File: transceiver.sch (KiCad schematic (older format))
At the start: 58 parts

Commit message: Updated with the ttl output
Adding a lot of footprints and other bits.
Changed TVS on USB
Added fuse on USB 5V
TTL level translators, 2x. Go from 3v3 to 1v8, then "anything" to 1v8
for the output.
2x LDO for 3v3->1v8, 3v3->2v5
Plus allow external input.
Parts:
- added C23, C24, C31, C32: 100nF, Capacitor_SMD:C_0603_1608Metric_Pad1.08x0.95mm_HandSolder, symbol Device:C_Small
- added J5: Conn_01x06_Male, Connector_PinHeader_2.54mm:PinHeader_1x06_P2.54mm_Vertical, symbol Connector:Conn_01x06_Male
- added J6, J7, J8: Conn_01x05_Male, Connector_PinHeader_2.54mm:PinHeader_1x05_P2.54mm_Vertical, symbol Connector:Conn_01x05_Male
- added JP15, JP16, JP17, JP18: Jumper, Connector_PinHeader_2.00mm:PinHeader_1x02_P2.00mm_Vertical_SMD_Pin1Left, symbol Device:Jumper
- added R15, R16, R17, R18, R19: 4k7, Connector_PinHeader_2.00mm:PinHeader_1x02_P2.00mm_Vertical_SMD_Pin1Left, symbol Device:R_Small
- added U12, U8: TXS0104EDR, Package_SO:SOIC-14_3.9x8.7mm_P1.27mm, symbol local:TXS0104EDR
- added U7: TLV75525PDBV, Package_TO_SOT_SMD:SOT-23-5, symbol Regulator_Linear:TLV75525PDBV
- added U9: TLV75518PDBV, Package_TO_SOT_SMD:SOT-23-5, symbol Regulator_Linear:TLV75518PDBV
- C19, C20, C21, C22, C25, C26, C27, C28, C29, C30, C33, C34, C35, C36, C37, C38, C39: renamed from C?; footprint (none) -> Capacitor_SMD:C_0603_1608Metric_Pad1.08x0.95mm_HandSolder
- J2, J3, J4, J9: renamed from J?; footprint (none) -> Connector_PinHeader_2.54mm:PinHeader_1x04_P2.54mm_Vertical
- JP1, JP10, JP11, JP12, JP13, JP14, JP19, JP2, JP20, JP21, JP22, JP23, JP24, JP25, JP26, JP3, JP4, JP5, JP6, JP7, JP8, JP9: renamed from JP?; footprint (none) -> Connector_PinHeader_2.00mm:PinHeader_1x02_P2.00mm_Vertical_SMD_Pin1Left
- R10, R11, R12, R13, R14, R9: renamed from R?; footprint (none) -> Connector_PinHeader_2.00mm:PinHeader_1x02_P2.00mm_Vertical_SMD_Pin1Left
- U10, U13, U4, U6: renamed from U?; footprint (none) -> Package_TO_SOT_SMD:SOT-23-6_Handsoldering
- U11, U5: renamed from U?; footprint TSSOP-24 -> Package_SO:TSSOP-24_4.4x7.8mm_P0.65mm
- gave numbers to parts that had none: 1
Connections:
- net +3V3: now also C23.1, JP17.1, R16.1, R17.1, U7.1 (IN), U7.3 (EN), U8.14 (VCCB), U9.1 (IN), U9.3 (EN)
- net CTSn_1: now also U8.10 (B4)
- net GND: now also C23.2, C24.2, C31.2, C32.2, J5.5 (Pin_5), J6.5 (Pin_5), J7.5 (Pin_5), J8.5 (Pin_5), R18.2, R19.2, U12.7 (GND), U7.2 (GND), U8.7 (GND), U9.2 (GND); no longer U13.1, U6.1
- net PORT_2_CTS: now also J6.4 (Pin_4)
- net PORT_2_RTS: now also J6.3 (Pin_3)
- net PORT_2_RXD: now also J6.2 (Pin_2)
- net PORT_2_TXD: now also J6.1 (Pin_1)
- net PORT_3_CTS: now also J7.4 (Pin_4)
- net PORT_3_RTS: now also J7.3 (Pin_3)
- net PORT_3_RXD: now also J7.2 (Pin_2)
- net PORT_3_TXD: now also J7.1 (Pin_1)
- net PORT_4_CTS: now also J8.4 (Pin_4)
- net PORT_4_RTS: now also J8.3 (Pin_3)
- net PORT_4_RXD: now also J8.2 (Pin_2)
- net PORT_4_TXD: now also J8.1 (Pin_1)
- net PWREN#: now also R17.2
- net RTSn_1: now also U8.11 (B3)
- net RXD_1: now also U8.12 (B2)
- net SUSPEND#: now also R16.2
- net TXD_1: now also U8.13 (B1)
- net DADBUS7 renamed DDBUS7
- new net: U12.2 (A1), U8.2 (A1)
- new net: U12.3 (A2), U8.3 (A2)
- new net: U12.4 (A3), U8.4 (A3)
- new net: U12.5 (A4), U8.5 (A4)
- new net: R15.2, U12.8 (OE), U8.8 (OE)
- new net: R18.1, U6.1
- new net: R19.1, U13.1
- new net +1V8: C24.1, C32.1, JP15.1, R15.1, U12.1 (VCCA), U8.1 (VCCA), U9.5 (OUT)
- new net +2V5: JP16.1, U7.5 (OUT)
- new net PORT_1_CTS: J5.4 (Pin_4), U12.10 (B4)
- new net PORT_1_RTS: J5.3 (Pin_3), U12.11 (B3)
- new net PORT_1_RXD: J5.2 (Pin_2), U12.12 (B2)
- new net PORT_1_TXD: J5.1 (Pin_1), U12.13 (B1)
- new net VBUS: JP18.1
- new net VREF: C31.1, J5.6 (Pin_6), JP15.2, JP16.2, JP17.2, JP18.2, U12.14 (VCCB)
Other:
- note added: "Convert the 3v3 Logic to 1v8, then we can do 1v8 to ANY upto 5V on the second stage."
- note added: "Gives direct TTL access\n3v3 bypassing level shifters"
- note added: "Maybe some screw terminals?"
- note added: "Need to generate 2v5 and 1v8 from 3v3\n3v3 and 5v are used as is. OR an external voltage can be used.\nIf no pins are jumpered, then external is the ref.\n\n"

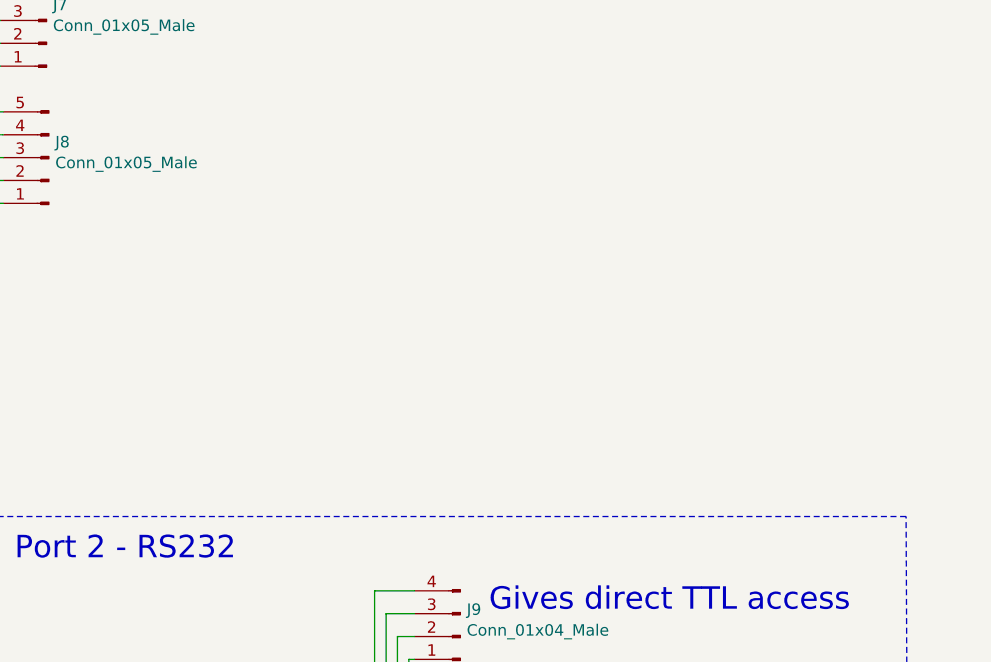
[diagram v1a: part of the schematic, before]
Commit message: Adding some LED stuff.
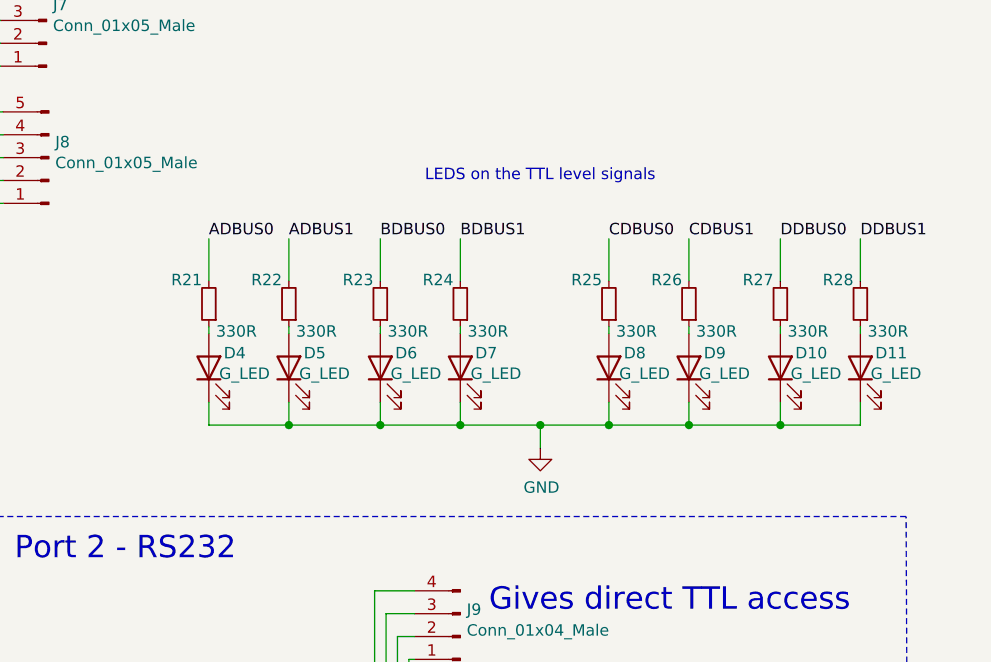
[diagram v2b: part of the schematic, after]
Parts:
- added D10, D11, D4, D5, D6, D7, D8, D9: G_LED, LED_SMD:LED_0603_1608Metric_Pad1.05x0.95mm_HandSolder, symbol Device:LED
- added R21, R22, R23, R24, R25, R26, R27, R28: 330R, Resistor_SMD:R_0603_1608Metric_Pad0.98x0.95mm_HandSolder, symbol Device:R_Small
- R10, R11, R12, R13, R14, R15, R16, R17, R18, R19, R9: footprint Connector_PinHeader_2.00mm:PinHeader_1x02_P2.00mm_Vertical_SMD_Pin1Left -> Resistor_SMD:R_0603_1608Metric_Pad0.98x0.95mm_HandSolder
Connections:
- net ADBUS0: now also R21.2
- net ADBUS1: now also R22.2
- net BDBUS0: now also R23.2
- net BDBUS1: now also R24.2
- net CDBUS0: now also R25.2
- net CDBUS1: now also R26.2
- net DDBUS0: now also R27.2
- net DDBUS1: now also R28.2
- net GND: now also D10.1 (K), D11.1 (K), D4.1 (K), D5.1 (K), D6.1 (K), D7.1 (K), D8.1 (K), D9.1 (K)
- new net: D11.2 (A), R28.1
- new net: D10.2 (A), R27.1
- new net: D9.2 (A), R26.1
- new net: D8.2 (A), R25.1
- new net: D7.2 (A), R24.1
- new net: D6.2 (A), R23.1
- new net: D5.2 (A), R22.1
- new net: D4.2 (A), R21.1
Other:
- note added: "LEDS on the TTL level signals"

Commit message: Added some footprints and started to look at layout
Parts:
- U14: footprint SnapEDA Library:SOP65P640X120-20N -> Package_SO:SO-20_12.8x7.5mm_P1.27mm
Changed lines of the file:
@@
 F 0 "U14" H 13975 9370 50  0000 C CNN
 F 1 "MAX3222EIPW" H 13975 9279 50  0000 C CNN
-F 2 "SnapEDA Library:SOP65P640X120-20N" H 13975 8300 50  0001 L BNN
+F 2 "Package_SO:SO-20_12.8x7.5mm_P1.27mm" H 13975 8300 50  0001 L BNN
 F 3 "https://www.ti.com/lit/gpn/max3222" H 13975 8300 50  0001 L BNN
 	1    13975 8300

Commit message: Updates as we do routing.
Changed discrete jumpres to a 2x4 block and 2x3 block, 2mm pitch.

Started routing each tranciever block
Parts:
- removed JP10, JP11, JP13, JP14, JP16, JP17, JP18, JP2, JP20, JP21, JP22, JP24, JP25, JP26, JP3, JP5, JP6, JP7, JP9: Jumper, Connector_PinHeader_2.00mm:PinHeader_1x02_P2.00mm_Vertical_SMD_Pin1Left, symbol Device:Jumper
- added JP27, JP28, JP29, JP30: Jumper, Connector_PinHeader_2.00mm:PinHeader_1x02_P2.00mm_Vertical_SMD_Pin1Left, symbol Device:Jumper
- added R31, R32, R33, R34: 120R, Resistor_SMD:R_0603_1608Metric_Pad0.98x0.95mm_HandSolder, symbol Device:R_Small
- JP1, JP12: footprint Connector_PinHeader_2.00mm:PinHeader_1x02_P2.00mm_Vertical_SMD_Pin1Left -> Connector_PinHeader_2.00mm:PinHeader_2x03_P2.00mm_Vertical_SMD; symbol Device:Jumper -> Connector_Generic:Conn_02x03_Odd_Even
- JP15: footprint Connector_PinHeader_2.00mm:PinHeader_1x02_P2.00mm_Vertical_SMD_Pin1Left -> Connector_PinHeader_1.27mm:PinHeader_2x04_P1.27mm_Vertical_SMD; symbol Device:Jumper -> Connector_Generic:Conn_02x04_Odd_Even
- JP19, JP23, JP4, JP8: footprint Connector_PinHeader_2.00mm:PinHeader_1x02_P2.00mm_Vertical_SMD_Pin1Left -> Connector_PinHeader_2.00mm:PinHeader_2x04_P2.00mm_Vertical_SMD; symbol Device:Jumper -> Connector_Generic:Conn_02x04_Odd_Even
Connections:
- net +2V5: now also JP15.3 (Pin_3)
- net +3V3: now also JP15.5 (Pin_5)
- net ADBUS0: now also JP4.7 (Pin_7); no longer JP4.1
- net ADBUS1: now also JP4.5 (Pin_5)
- net ADBUS2: now also JP4.3 (Pin_3)
- net ADBUS3: now also JP4.1 (Pin_1)
- net BDBUS1: now also JP23.3 (Pin_3)
- net BDBUS2: now also JP23.5 (Pin_5)
- net BDBUS3: now also JP23.7 (Pin_7)
- net CDBUS1: now also JP8.3 (Pin_3)
- net CDBUS2: now also JP8.5 (Pin_5)
- net CDBUS3: now also JP8.7 (Pin_7)
- net CTSn_1: now also JP4.2 (Pin_2)
- net CTSn_2: now also JP23.8 (Pin_8)
- net CTSn_3: now also JP8.8 (Pin_8)
- net CTSn_4: now also JP19.8 (Pin_8)
- net DDBUS1: now also JP19.3 (Pin_3)
- net DDBUS2: now also JP19.5 (Pin_5)
- net DDBUS3: now also JP19.7 (Pin_7)
- net FULLn_3: now also JP1.4 (Pin_4)
- net FULLn_4: now also JP12.4 (Pin_4)
- net GND: now also JP1.3 (Pin_3), JP1.5 (Pin_5), JP12.3 (Pin_3), JP12.5 (Pin_5)
- net PORT_3_CTS: now also R33.2
- net PORT_3_RTS: now also R31.2
- net PORT_3_RXD: now also JP29.2
- net PORT_3_TXD: now also JP27.2
- net PORT_4_CTS: now also R34.2
- net PORT_4_RTS: now also R32.2
- net PORT_4_RXD: now also JP30.2
- net PORT_4_TXD: now also JP28.2
- net RTSn_1: now also JP4.4 (Pin_4)
- net RTSn_2: now also JP23.6 (Pin_6)
- net RTSn_3: now also JP8.6 (Pin_6)
- net RTSn_4: now also JP19.6 (Pin_6)
- net RXD_1: now also JP4.6 (Pin_6)
- net RXD_2: now also JP23.4 (Pin_4)
- net RXD_3: now also JP8.4 (Pin_4)
- net RXD_4: now also JP19.4 (Pin_4)
- net TXD_1: now also JP4.8 (Pin_8); no longer JP4.2
- net VBUS: now also JP15.7 (Pin_7)
- net at R11.2, U5.12 (*SLEW): now also JP1.6 (Pin_6)
- net at R14.2, U11.12 (*SLEW): now also JP12.6 (Pin_6)
- net VREF renamed Vdrive
- net Vdrive: now also JP15.4 (Pin_4), JP15.6 (Pin_6), JP15.8 (Pin_8)
- new net: JP27.1, R31.1
- new net: JP28.1, R32.1
- new net: JP29.1, R33.1
- new net: JP30.1, R34.1
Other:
- note added: "1.27mm 2pin headers - Disconnect XCVR\n"
- note added: "Termination resistors for the rs485\nPorts 3 & 4"

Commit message: Almost fully routed.. lots of DRC's to sort out.
Also need to get correct pcb parameters to do more checks.
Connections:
- net ADBUS0: now also J3.1 (Pin_1), JP8.1 (Pin_1), R25.2; no longer J2.1 (Pin_1), JP4.7 (Pin_7), R21.2
- net ADBUS1: now also J3.2 (Pin_2), JP8.3 (Pin_3), R26.2; no longer J2.2 (Pin_2), JP4.5 (Pin_5), R22.2
- net ADBUS2: now also J3.3 (Pin_3), JP8.5 (Pin_5); no longer J2.3 (Pin_3), JP4.3 (Pin_3)
- net ADBUS3: now also J3.4 (Pin_4), JP8.7 (Pin_7); no longer J2.4 (Pin_4), JP4.1 (Pin_1)
- net ADBUS7: now also U4.1, U6.3
- net BDBUS0: now also J2.1 (Pin_1), JP4.7 (Pin_7), R21.2; no longer J9.1 (Pin_1), JP23.1 (Pin_1), R23.2
- net BDBUS1: now also J2.2 (Pin_2), JP4.5 (Pin_5), R22.2; no longer J9.2 (Pin_2), JP23.3 (Pin_3), R24.2
- net BDBUS2: now also J2.3 (Pin_3), JP4.3 (Pin_3); no longer J9.3 (Pin_3), JP23.5 (Pin_5)
- net BDBUS3: now also J2.4 (Pin_4), JP4.1 (Pin_1); no longer J9.4 (Pin_4), JP23.7 (Pin_7)
- net CDBUS0: now also J9.1 (Pin_1), JP23.1 (Pin_1), R23.2; no longer J3.1 (Pin_1), JP8.1 (Pin_1), R25.2
- net CDBUS1: now also J9.2 (Pin_2), JP23.3 (Pin_3), R24.2; no longer J3.2 (Pin_2), JP8.3 (Pin_3), R26.2
- net CDBUS2: now also J9.3 (Pin_3), JP23.5 (Pin_5); no longer J3.3 (Pin_3), JP8.5 (Pin_5)
- net CDBUS3: now also J9.4 (Pin_4), JP23.7 (Pin_7); no longer J3.4 (Pin_4), JP8.7 (Pin_7)
- net CDBUS7: no longer U4.1, U6.3
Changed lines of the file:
@@
 Wire Bus Line
 	6875 5825 7275 5825
-Text GLabel 1075 2750 0    50   Input ~ 0
+Text GLabel 1125 2825 0    50   Input ~ 0
+BDBUS[0..7]
+Text GLabel 12575 5300 0    50   Input ~ 0
+CDBUS[0..7]
+Text GLabel 1575 5950 0    50   Input ~ 0
 ADBUS[0..7]
-Text GLabel 12575 5300 0    50   Input ~ 0
-BDBUS[0..7]
-Text GLabel 1575 5950 0    50   Input ~ 0
-CDBUS[0..7]
 Text GLabel 6875 5825 0    50   Input ~ 0
 DDBUS[0..7]
@@
 	1625 3875 2025 3875
 Text Label 1700 3175 0    50   ~ 0
-ADBUS0
+BDBUS0
 Text Label 1700 3275 0    50   ~ 0
-ADBUS1
+BDBUS1
 Text Label 1700 3375 0    50   ~ 0
-ADBUS2
+BDBUS2
 Text Label 1700 3475 0    50   ~ 0
-ADBUS3
+BDBUS3
 Text Label 1700 3575 0    50   ~ 0
-ADBUS4
+BDBUS4
 Text Label 1700 3675 0    50   ~ 0
-ADBUS5
+BDBUS5
 Text Label 1700 3775 0    50   ~ 0
-ADBUS6
+BDBUS6
 Text Label 1700 3875 0    50   ~ 0
-ADBUS7
+BDBUS7
 Text Notes 575  1900 0    98   ~ 0
 Mapping of Bus to Serial\n0: TXD\n1: RXD\n2: RTSn\n3: CTSn\n4: DTRn\n5: DSRn\n6: DCDn\n7: TXDEN
-Text Notes 2725 1150 0    98   ~ 0
-BUSA: CMOS/TTL\nBUSB: RS232\nBUSC: RS422/485/RS232\nBUSC: RS422/485/RS232\n
 $Comp
 L Connector_Generic:Conn_02x04_Odd_Even JP4
@@
 	13075 6350 13475 6350
 Text Label 13150 5650 0    50   ~ 0
-BDBUS0
+CDBUS0
 Text Label 13150 5750 0    50   ~ 0
-BDBUS1
+CDBUS1
 Text Label 13150 5850 0    50   ~ 0
-BDBUS2
+CDBUS2
 Text Label 13150 5950 0    50   ~ 0
-BDBUS3
+CDBUS3
 Text Label 13150 6050 0    50   ~ 0
-BDBUS4
+CDBUS4
 Text Label 13150 6150 0    50   ~ 0
-BDBUS5
+CDBUS5
 Text Label 13150 6250 0    50   ~ 0
-BDBUS6
+CDBUS6
 Text Label 13150 6350 0    50   ~ 0
-BDBUS7
+CDBUS7
 $Comp
 L Connector_Generic:Conn_02x04_Odd_Even JP23
@@
 NoConn ~ 13475 6250
 NoConn ~ 13475 6350
-Wire Wire Line
-	14550 5650 14650 5650
-Wire Wire Line
-	14550 5750 14650 5750
-Wire Wire Line
-	14550 5850 14650 5850
-Wire Wire Line
-	14550 5950 14650 5950
 Text Label 14700 5650 0    50   ~ 0
 TXD_2
@@
 	2075 6900 2475 6900
 Text Label 2150 6300 0    50   ~ 0
-CDBUS0
+ADBUS0
 Text Label 2150 6400 0    50   ~ 0
-CDBUS1
+ADBUS1
 Text Label 2150 6500 0    50   ~ 0
-CDBUS2
+ADBUS2
 Text Label 2150 6600 0    50   ~ 0
-CDBUS3
+ADBUS3
 Text Label 2150 6700 0    50   ~ 0
-CDBUS4
+ADBUS4
 Text Label 2150 6800 0    50   ~ 0
-CDBUS5
+ADBUS5
 Text Label 2150 6900 0    50   ~ 0
-CDBUS6
+ADBUS6
 Text Label 2150 7000 0    50   ~ 0
-CDBUS7
+ADBUS7
 $Comp
 L Connector_Generic:Conn_02x04_Odd_Even JP8
@@
 Connection ~ 13100 4100
 Text Label 12750 3285 0    50   ~ 0
+BDBUS0
+Text Label 13100 3285 0    50   ~ 0
+BDBUS1
+Text Label 13850 3285 0    50   ~ 0
+CDBUS1
+Text Label 13500 3285 0    50   ~ 0
+CDBUS0
+Text Label 14850 3285 0    50   ~ 0
+ADBUS1
+Text Label 14500 3285 0    50   ~ 0
 ADBUS0
-Text Label 13100 3285 0    50   ~ 0
-ADBUS1
-Text Label 13850 3285 0    50   ~ 0
-BDBUS1
-Text Label 13500 3285 0    50   ~ 0
-BDBUS0
-Text Label 14850 3285 0    50   ~ 0
-CDBUS1
-Text Label 14500 3285 0    50   ~ 0
-CDBUS0
 Text Label 15600 3285 0    50   ~ 0
 DDBUS1
@@
 Wire Wire Line
 	11750 830  11840 830
-Connection ~ 14650 5650
-Wire Wire Line
-	14650 5650 14700 5650
-Connection ~ 14650 5750
-Wire Wire Line
-	14650 5750 14700 5750
-Connection ~ 14650 5850
-Wire Wire Line
-	14650 5850 14700 5850
-Connection ~ 14650 5950
-Wire Wire Line
-	14650 5950 14700 5950
+Wire Wire Line
+	14550 5650 14700 5650
+Wire Wire Line
+	14550 5750 14700 5750
+Wire Wire Line
+	14550 5850 14700 5850
+Wire Wire Line
+	14550 5950 14700 5950
 Wire Bus Line
 	7275 5825 7275 6775
@@
 Wire Bus Line
 	1525 2825 1525 3775
+Text Notes 2760 1155 0    98   ~ 0
+BUSA: CMOS/TTL\nBUSB: RS232\nBUSC: RS422/485/RS232\nBUSC: RS422/485/RS232\n
 $EndSCHEMATC
